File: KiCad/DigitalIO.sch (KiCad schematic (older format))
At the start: 114 parts, among them J201 TE_Connectivity_1-282834-0, J202 TE_Connectivity_282834-6, J203 GS3, J204 GS3, J205 GS3, J206 GS3, J207 GS3, J208 GS3, J209 GS3, J210 GS3, J211 TE_Connectivity_282834-6, J212 TE_Connectivity_1-282834-0, Q201 ZXTN25050DFHTA, Q202 ZXTN25050DFHTA, Q203 ZXTN25050DFHTA, Q204 ZXTN25050DFHTA, Q205 ZXTN25050DFHTA, Q206 ZXTN25050DFHTA, Q207 ZXTN25050DFHTA, Q208 ZXTN25050DFHTA, U201 LTV-354T, U202 LTV-354T, U203 LTV-354T, U204 LTV-354T, U205 LTV-354T, U206 LTV-354T, U207 LTV-354T, U208 LTV-354T, U209 MCP23017

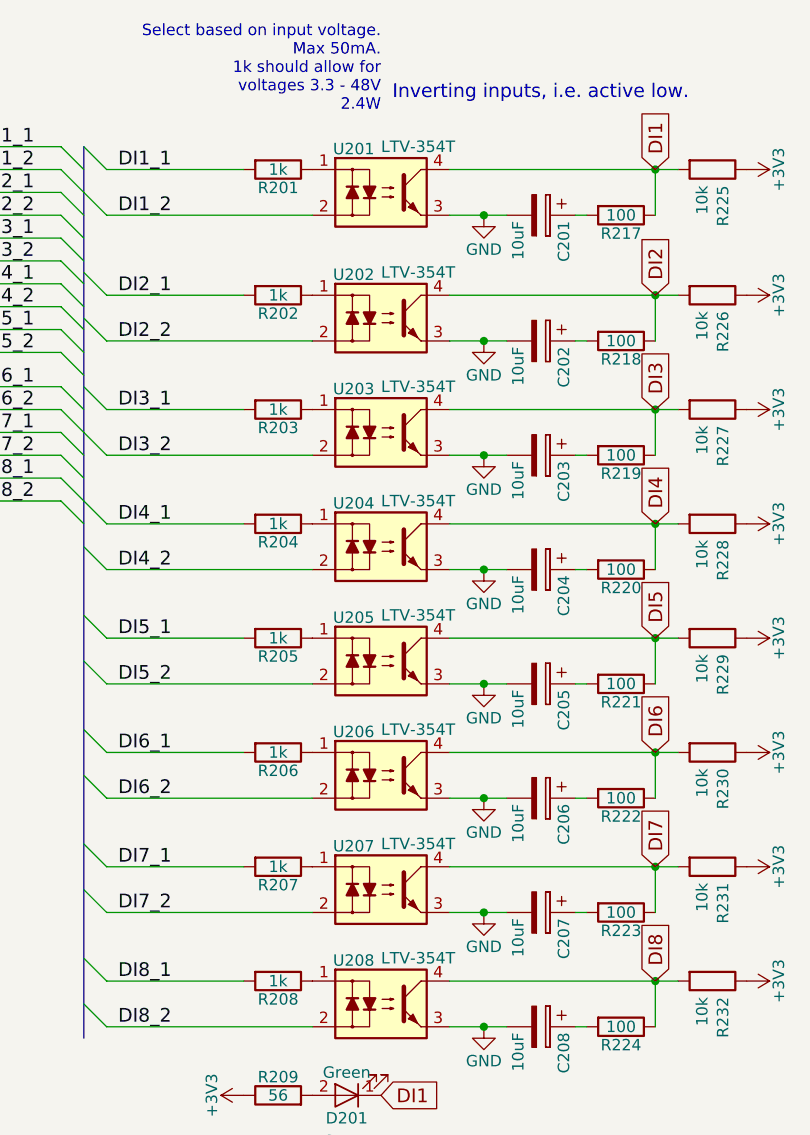
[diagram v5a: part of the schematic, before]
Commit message: New sense input circuits. New layout
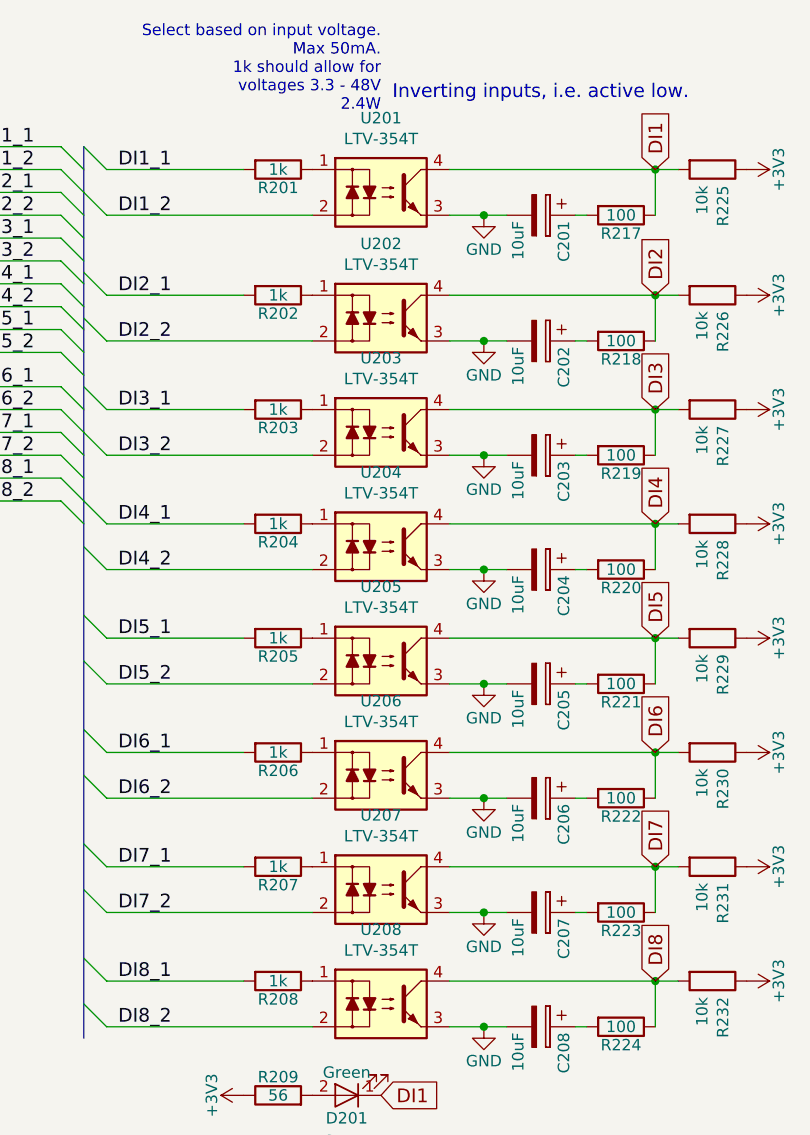
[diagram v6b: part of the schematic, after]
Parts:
- U201, U202, U203, U204, U205, U206, U207, U208: footprint LTV-354T_MiniFlat:LTV-354T_MiniFlat -> Housings_SOIC:SO-4_4.4x3.6mm_Pitch2.54mm
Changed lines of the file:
@@
-$EndComp
-$Comp
-L LTV-354T U208
-U 1 1 59181E44
-P 3000 5000
-F 0 "U208" H 2790 5190 50  0000 L CNN
-F 1 "LTV-354T" H 3000 5200 50  0000 L CNN
-F 2 "LTV-354T_MiniFlat:LTV-354T_MiniFlat" H 2800 4800 50  0001 L CIN
-F 3 "" H 3025 5000 50  0001 L CNN
-	1    3000 5000
-	1    0    0    -1
-$EndComp
-$Comp
-L LTV-354T U207
-U 1 1 59181E59
-P 3000 4500
-F 0 "U207" H 2790 4690 50  0000 L CNN
-F 1 "LTV-354T" H 3000 4700 50  0000 L CNN
-F 2 "LTV-354T_MiniFlat:LTV-354T_MiniFlat" H 2800 4300 50  0001 L CIN
-F 3 "" H 3025 4500 50  0001 L CNN
-	1    3000 4500
-	1    0    0    -1
-$EndComp
-$Comp
-L LTV-354T U206
-U 1 1 59181E6E
-P 3000 4000
-F 0 "U206" H 2790 4190 50  0000 L CNN
-F 1 "LTV-354T" H 3000 4200 50  0000 L CNN
-F 2 "LTV-354T_MiniFlat:LTV-354T_MiniFlat" H 2800 3800 50  0001 L CIN
-F 3 "" H 3025 4000 50  0001 L CNN
-	1    3000 4000
-	1    0    0    -1
-$EndComp
-$Comp
-L LTV-354T U205
-U 1 1 59181E83
-P 3000 3500
-F 0 "U205" H 2790 3690 50  0000 L CNN
-F 1 "LTV-354T" H 3000 3700 50  0000 L CNN
-F 2 "LTV-354T_MiniFlat:LTV-354T_MiniFlat" H 2800 3300 50  0001 L CIN
-F 3 "" H 3025 3500 50  0001 L CNN
-	1    3000 3500
-	1    0    0    -1
-$EndComp
-$Comp
-L LTV-354T U204
-U 1 1 59181E98
-P 3000 3000
-F 0 "U204" H 2790 3190 50  0000 L CNN
-F 1 "LTV-354T" H 3000 3200 50  0000 L CNN
-F 2 "LTV-354T_MiniFlat:LTV-354T_MiniFlat" H 2800 2800 50  0001 L CIN
-F 3 "" H 3025 3000 50  0001 L CNN
-	1    3000 3000
-	1    0    0    -1
-$EndComp
-$Comp
-L LTV-354T U203
-U 1 1 59181EAD
-P 3000 2500
-F 0 "U203" H 2790 2690 50  0000 L CNN
-F 1 "LTV-354T" H 3000 2700 50  0000 L CNN
-F 2 "LTV-354T_MiniFlat:LTV-354T_MiniFlat" H 2800 2300 50  0001 L CIN
-F 3 "" H 3025 2500 50  0001 L CNN
-	1    3000 2500
-	1    0    0    -1
-$EndComp
-$Comp
-L LTV-354T U202
-U 1 1 59181EC2
-P 3000 2000
-F 0 "U202" H 2790 2190 50  0000 L CNN
-F 1 "LTV-354T" H 3000 2200 50  0000 L CNN
-F 2 "LTV-354T_MiniFlat:LTV-354T_MiniFlat" H 2800 1800 50  0001 L CIN
-F 3 "" H 3025 2000 50  0001 L CNN
-	1    3000 2000
-	1    0    0    -1
 $EndComp
 $Comp
@@
 F 3 "" H 3450 1550 50  0001 C CNN
 	1    3450 1550
-	1    0    0    -1
-$EndComp
-$Comp
-L LTV-354T U201
-U 1 1 59181EFB
-P 3000 1450
-F 0 "U201" H 2790 1640 50  0000 L CNN
-F 1 "LTV-354T" H 3000 1650 50  0000 L CNN
-F 2 "LTV-354T_MiniFlat:LTV-354T_MiniFlat" H 2800 1250 50  0001 L CIN
-F 3 "" H 3025 1450 50  0001 L CNN
-	1    3000 1450
 	1    0    0    -1
 $EndComp
@@
 	0    -1   -1   0
 $EndComp
+$Comp
+L LTV-354T U201
+U 1 1 59363A8D
+P 3000 1450
+F 0 "U201" H 3000 1775 50  0000 C CNN
+F 1 "LTV-354T" H 3000 1684 50  0000 C CNN
+F 2 "Housings_SOIC:SO-4_4.4x3.6mm_Pitch2.54mm" H 2800 1250 50  0001 L CIN
+F 3 "" H 3025 1450 50  0001 L CNN
+	1    3000 1450
+	1    0    0    -1
+$EndComp
+$Comp
+L LTV-354T U202
+U 1 1 5936620E
+P 3000 2000
+F 0 "U202" H 3000 2325 50  0000 C CNN
+F 1 "LTV-354T" H 3000 2234 50  0000 C CNN
+F 2 "Housings_SOIC:SO-4_4.4x3.6mm_Pitch2.54mm" H 2800 1800 50  0001 L CIN
+F 3 "" H 3025 2000 50  0001 L CNN
+	1    3000 2000
+	1    0    0    -1
+$EndComp
+$Comp
+L LTV-354T U203
+U 1 1 59366306
+P 3000 2500
+F 0 "U203" H 3000 2825 50  0000 C CNN
+F 1 "LTV-354T" H 3000 2734 50  0000 C CNN
+F 2 "Housings_SOIC:SO-4_4.4x3.6mm_Pitch2.54mm" H 2800 2300 50  0001 L CIN
+F 3 "" H 3025 2500 50  0001 L CNN
+	1    3000 2500
+	1    0    0    -1
+$EndComp
+$Comp
+L LTV-354T U204
+U 1 1 59366400
+P 3000 3000
+F 0 "U204" H 3000 3325 50  0000 C CNN
+F 1 "LTV-354T" H 3000 3234 50  0000 C CNN
+F 2 "Housings_SOIC:SO-4_4.4x3.6mm_Pitch2.54mm" H 2800 2800 50  0001 L CIN
+F 3 "" H 3025 3000 50  0001 L CNN
+	1    3000 3000
+	1    0    0    -1
+$EndComp
+$Comp
+L LTV-354T U205
+U 1 1 59366B70
+P 3000 3500
+F 0 "U205" H 3000 3825 50  0000 C CNN
+F 1 "LTV-354T" H 3000 3734 50  0000 C CNN
+F 2 "Housings_SOIC:SO-4_4.4x3.6mm_Pitch2.54mm" H 2800 3300 50  0001 L CIN
+F 3 "" H 3025 3500 50  0001 L CNN
+	1    3000 3500
+	1    0    0    -1
+$EndComp
+$Comp
+L LTV-354T U206
+U 1 1 59366C74
+P 3000 4000
+F 0 "U206" H 3000 4325 50  0000 C CNN
+F 1 "LTV-354T" H 3000 4234 50  0000 C CNN
+F 2 "Housings_SOIC:SO-4_4.4x3.6mm_Pitch2.54mm" H 2800 3800 50  0001 L CIN
+F 3 "" H 3025 4000 50  0001 L CNN
+	1    3000 4000
+	1    0    0    -1
+$EndComp
+$Comp
+L LTV-354T U207
+U 1 1 59366D74
+P 3000 4500
+F 0 "U207" H 3000 4825 50  0000 C CNN
+F 1 "LTV-354T" H 3000 4734 50  0000 C CNN
+F 2 "Housings_SOIC:SO-4_4.4x3.6mm_Pitch2.54mm" H 2800 4300 50  0001 L CIN
+F 3 "" H 3025 4500 50  0001 L CNN
+	1    3000 4500
+	1    0    0    -1
+$EndComp
+$Comp
+L LTV-354T U208
+U 1 1 5936790E
+P 3000 5000
+F 0 "U208" H 3000 5325 50  0000 C CNN
+F 1 "LTV-354T" H 3000 5234 50  0000 C CNN
+F 2 "Housings_SOIC:SO-4_4.4x3.6mm_Pitch2.54mm" H 2800 4800 50  0001 L CIN
+F 3 "" H 3025 5000 50  0001 L CNN
+	1    3000 5000
+	1    0    0    -1
+$EndComp
 $EndSCHEMATC
